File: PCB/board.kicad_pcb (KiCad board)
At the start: 2 copper layers, 28 parts, among them J1 USB TYPE-B FEMALE, J2 SPI, J3 Conn_01x05_Male, J4 Power, SW1 SW_Push, SW2 SW_Push, U1 PIC18F2550-ISP, U2 AMS1117-3.3, U3 NRF24L01_Breakout, Y1 8Mhz

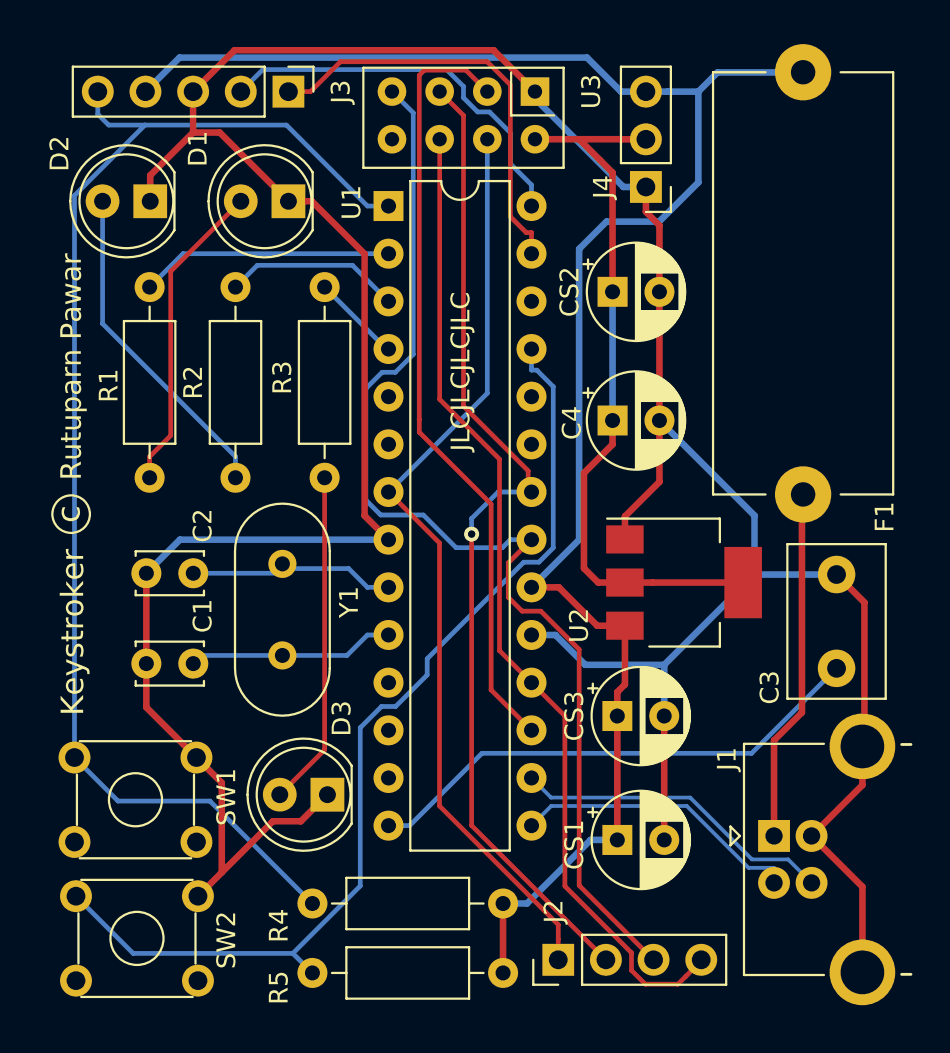
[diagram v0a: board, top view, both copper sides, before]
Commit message: BOM and PCB 3D render added
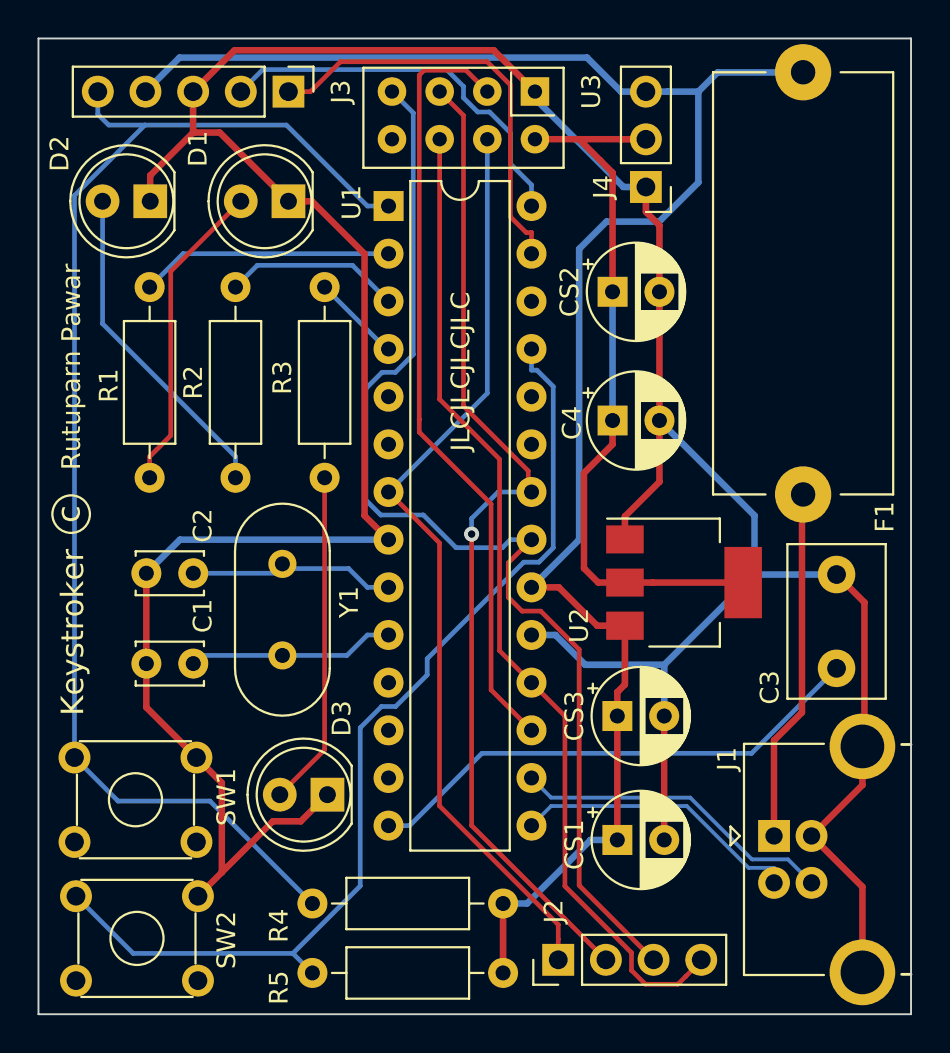
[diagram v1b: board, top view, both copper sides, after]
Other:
- board outline added: 46.5 x 52 mm
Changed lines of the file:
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@@
   (general
     (thickness 1.6)
-    (drawings 12)
+    (drawings 16)
     (tracks 240)
     (zones 0)
@@
     (42 Eco1.User user hide)
     (43 Eco2.User user hide)
-    (44 Edge.Cuts user hide)
+    (44 Edge.Cuts user)
     (45 Margin user hide)
     (46 B.CrtYd user)
@@
     (pad 2 thru_hole circle (at 22.5 0 270) (size 3 3) (drill 1.3) (layers *.Cu *.Mask)
       (net 33 "Net-(J1-Pad1)"))
-    (model ${KISYS3DMOD}/Fuse.3dshapes/Fuseholder_Cylinder-5x20mm_Schurter_0031_8201_Horizontal_Open.wrl
-      (at (xyz 0 0 0))
+    (model ${KIPRJMOD}/board.3dshapes/spst_switch.step
+      (offset (xyz 10.5 -4.5 5.5))
       (scale (xyz 1 1 1))
       (rotate (xyz 0 0 0))
@@
     (pad 5 thru_hole circle (at 4.71 7.27) (size 3.5 3.5) (drill 2.33) (layers *.Cu *.Mask)
       (net 1 GND))
-    (model ${KISYS3DMOD}/Connector_USB.3dshapes/USB_B_OST_USB-B1HSxx_Horizontal.wrl
-      (at (xyz 0 0 0))
-      (scale (xyz 1 1 1))
-      (rotate (xyz 0 0 0))
+    (model ${KIPRJMOD}/board.3dshapes/usb_type_b_receptacle.step
+      (offset (xyz 14.5 -1 0))
+      (scale (xyz 1 1 1))
+      (rotate (xyz -90 0 -90))
     )
   )
@@
     )
   )
+  (dimension 46.5 (width 0.15) (layer Dwgs.User)
+    (gr_text "46.500 mm" (at 109.75 58.7) (layer Dwgs.User)
+      (effects (font (size 1 1) (thickness 0.15)))
+    )
+    (feature1 (pts (xy 86.5 66) (xy 86.5 59.413579)))
+    (feature2 (pts (xy 133 66) (xy 133 59.413579)))
+    (crossbar (pts (xy 133 60) (xy 86.5 60)))
+    (arrow1a (pts (xy 86.5 60) (xy 87.626504 59.413579)))
+    (arrow1b (pts (xy 86.5 60) (xy 87.626504 60.586421)))
+    (arrow2a (pts (xy 133 60) (xy 131.873496 59.413579)))
+    (arrow2b (pts (xy 133 60) (xy 131.873496 60.586421)))
+  )
+  (gr_line (start 133 118) (end 133 66) (layer Dwgs.User) (width 0.15))
+  (gr_line (start 133 66) (end 133 118) (layer Edge.Cuts) (width 0.1))
+  (gr_line (start 133 66) (end 86.5 66) (layer Dwgs.User) (width 0.15))
+  (gr_line (start 86.5 66) (end 133 66) (layer Edge.Cuts) (width 0.1))
+  (dimension 52 (width 0.15) (layer Dwgs.User)
+    (gr_text "52.000 mm" (at 79.7 92 90) (layer Dwgs.User)
+      (effects (font (size 1 1) (thickness 0.15)))
+    )
+    (feature1 (pts (xy 86.5 66) (xy 80.413579 66)))
+    (feature2 (pts (xy 86.5 118) (xy 80.413579 118)))
+    (crossbar (pts (xy 81 118) (xy 81 66)))
+    (arrow1a (pts (xy 81 66) (xy 81.586421 67.126504)))
+    (arrow1b (pts (xy 81 66) (xy 80.413579 67.126504)))
+    (arrow2a (pts (xy 81 118) (xy 81.586421 116.873496)))
+    (arrow2b (pts (xy 81 118) (xy 80.413579 116.873496)))
+  )
+  (gr_line (start 86.5 118) (end 133 118) (layer Dwgs.User) (width 0.15))
+  (gr_line (start 86.5 66) (end 86.5 118) (layer Dwgs.User) (width 0.15))
+  (gr_line (start 86.5 118) (end 86.5 66) (layer Edge.Cuts) (width 0.1))
+  (gr_line (start 133 118) (end 86.5 118) (layer Edge.Cuts) (width 0.1))
   (gr_text Keystroker (at 88.325 97.65 90) (layer F.SilkS)
     (effects (font (size 1.2 1.2) (thickness 0.15)))
@@
   )
   (gr_text "Rutuparn Pawar" (at 88.25 83.5 90) (layer F.SilkS)
-    (effects (font (size 1.1 1.1) (thickness 0.15)))
-  )
-  (dimension 51.800004 (width 0.15) (layer Dwgs.User)
-    (gr_text "51.800 mm" (at 79.30958 91.937274 89.97787808) (layer Dwgs.User)
-      (effects (font (size 1 1) (thickness 0.15)))
-    )
-    (feature1 (pts (xy 86.36 117.84) (xy 80.01316 117.837549)))
-    (feature2 (pts (xy 86.38 66.04) (xy 80.03316 66.037549)))
-    (crossbar (pts (xy 80.61958 66.037776) (xy 80.59958 117.837776)))
-    (arrow1a (pts (xy 80.59958 117.837776) (xy 80.013594 116.711046)))
-    (arrow1b (pts (xy 80.59958 117.837776) (xy 81.186436 116.711499)))
-    (arrow2a (pts (xy 80.61958 66.037776) (xy 80.032724 67.164053)))
-    (arrow2b (pts (xy 80.61958 66.037776) (xy 81.205566 67.164506)))
-  )
-  (dimension 46.710001 (width 0.15) (layer Dwgs.User)
-    (gr_text "46.710 mm" (at 109.736477 59.145234 359.9877337) (layer Dwgs.User)
-      (effects (font (size 1 1) (thickness 0.15)))
-    )
-    (feature1 (pts (xy 133.09 66.05) (xy 133.091324 59.863813)))
-    (feature2 (pts (xy 86.38 66.04) (xy 86.381324 59.853813)))
-    (crossbar (pts (xy 86.381199 60.440234) (xy 133.091199 60.450234)))
-    (arrow1a (pts (xy 133.091199 60.450234) (xy 131.96457 61.036414)))
-    (arrow1b (pts (xy 133.091199 60.450234) (xy 131.964821 59.863572)))
-    (arrow2a (pts (xy 86.381199 60.440234) (xy 87.507577 61.026896)))
-    (arrow2b (pts (xy 86.381199 60.440234) (xy 87.507828 59.854054)))
-  )
-  (gr_line (start 133.09 66.05) (end 133.08 117.85) (layer Dwgs.User) (width 0.15))
+    (effects (font (size 1 1) (thickness 0.15)))
+  )
   (gr_line (start 132.5 115.875) (end 133 115.875) (layer F.SilkS) (width 0.15))
   (gr_line (start 132.5 103.625) (end 133 103.625) (layer F.SilkS) (width 0.15))
@@
     (effects (font (size 1 1) (thickness 0.15)))
   )
-  (gr_line (start 86.36 117.84) (end 133.08 117.85) (layer Dwgs.User) (width 0.15))
-  (gr_line (start 86.38 66.04) (end 86.36 117.84) (layer Dwgs.User) (width 0.15))
-  (gr_line (start 133.09 66.05) (end 86.38 66.04) (layer Dwgs.User) (width 0.15))
   (segment (start 124.6599 94.568) (end 129.032 94.568) (width 0.35) (layer B.Cu) (net 1))
   (segment (start 119.848 99.3799) (end 124.6599 94.568) (width 0.35) (layer B.Cu) (net 1))

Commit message: Ground plane added to PCB
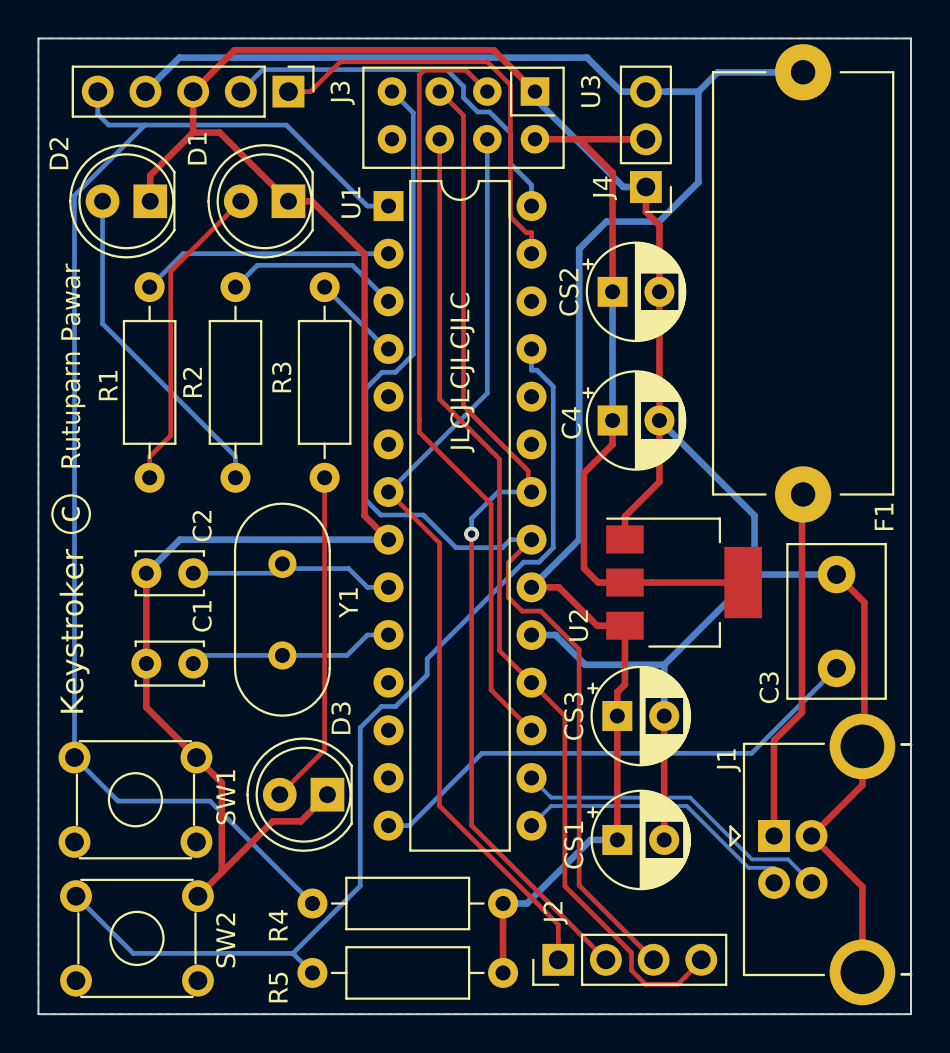
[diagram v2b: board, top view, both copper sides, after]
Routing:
- added copper zone on B.Cu, net GND
- added copper zone on F.Cu, net GND
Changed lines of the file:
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@@
   (segment (start 125.7 103.408) (end 125.7 108.5) (width 0.35) (layer F.Cu) (net 33))
   (segment (start 127.19 101.918) (end 125.7 103.408) (width 0.35) (layer F.Cu) (net 33))
+  (zone (net 1) (net_name GND) (layer F.Cu) (hatch edge 0.508)
+    (connect_pads (clearance 0.508))
+    (min_thickness 0.254)
+    (fill yes (arc_segments 32) (thermal_gap 0.508) (thermal_bridge_width 0.508))
+    (polygon
+      (pts
+        (xy 86.5 66) (xy 133 66) (xy 133 118) (xy 86.5 118)
+      )
+    )
+  )
+  (zone (net 1) (net_name GND) (layer B.Cu) (hatch edge 0.508)
+    (connect_pads (clearance 0.508))
+    (min_thickness 0.254)
+    (fill yes (arc_segments 32) (thermal_gap 0.508) (thermal_bridge_width 0.508))
+    (polygon
+      (pts
+        (xy 86.5 66) (xy 133 66) (xy 133 118) (xy 86.5 118)
+      )
+    )
+  )
 )
